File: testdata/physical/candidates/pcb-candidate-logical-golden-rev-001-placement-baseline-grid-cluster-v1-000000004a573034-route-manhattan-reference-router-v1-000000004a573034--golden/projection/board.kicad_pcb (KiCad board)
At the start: 2 copper layers, 60 x 40 mm, 6 parts

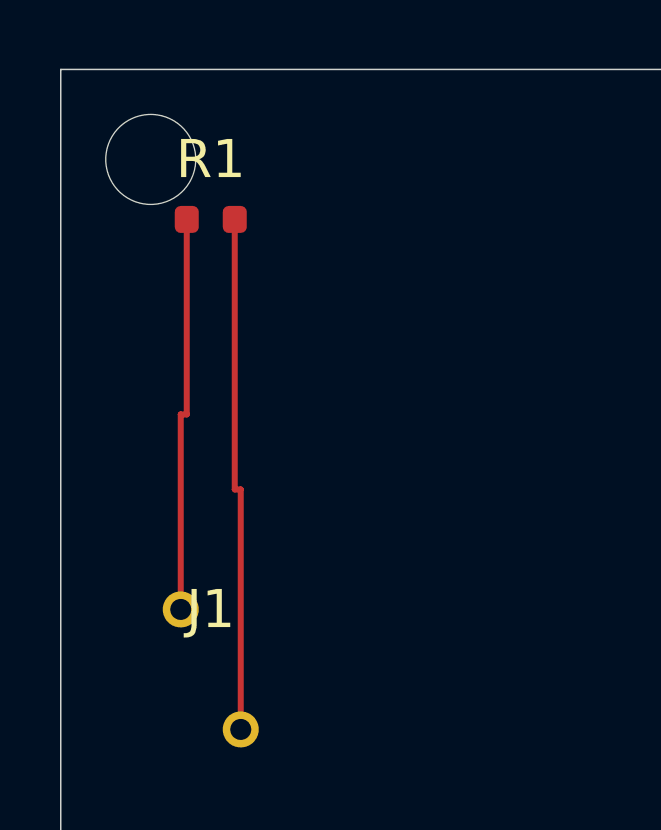
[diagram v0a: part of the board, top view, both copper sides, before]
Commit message: fix(pcb): pass pinned KiCad 10 fabrication gates
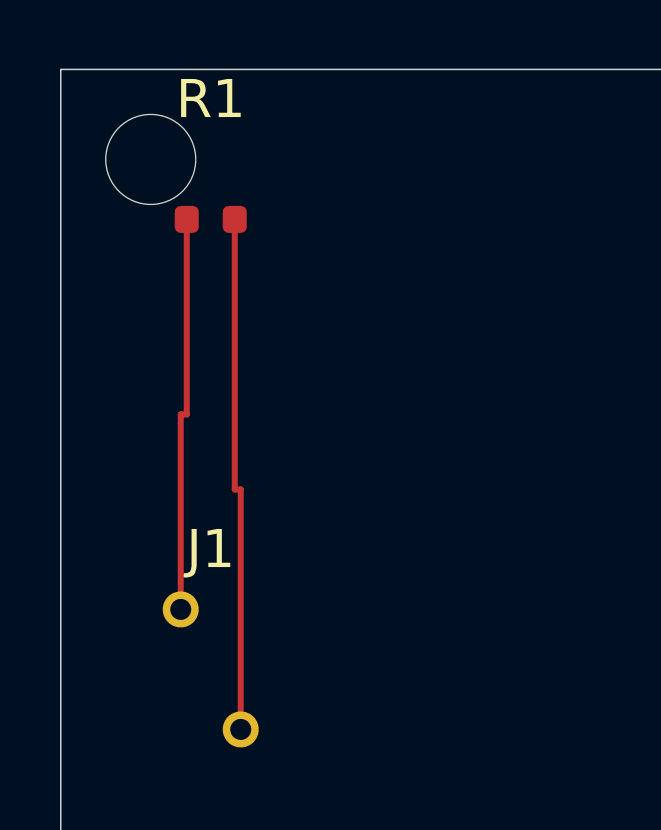
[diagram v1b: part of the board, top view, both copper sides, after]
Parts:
- ? (x4): footprint Jingwei:MechanicalHole -> (none)
- J1: footprint Jingwei:CONN_2P_2.54 -> (none)
- R1: footprint Jingwei:R_0603_1608Metric -> (none)
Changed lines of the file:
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@@
-(kicad_pcb (version 20240108) (generator jingwei-agent) (generator_version "jingwei-kicad-pcb-v1") (general (thickness 1.6)) (layers (0 "F.Cu" signal) (2 "B.Cu" signal) (36 "F.Mask" user) (37 "B.Mask" user) (37 "F.SilkS" user) (36 "B.SilkS" user) (44 "Edge.Cuts" user)) (setup) (net 1 "GND") (net 2 "+3V3") (gr_line (start 0 0) (end 60 0) (stroke (width 0.05)) (layer "Edge.Cuts")) (gr_line (start 60 0) (end 60 40) (stroke (width 0.05)) (layer "Edge.Cuts")) (gr_line (start 60 40) (end 0 40) (stroke (width 0.05)) (layer "Edge.Cuts")) (gr_line (start 0 40) (end 0 0) (stroke (width 0.05)) (layer "Edge.Cuts")) (footprint "Jingwei:MechanicalHole" (layer "F.Cu") (at 3 3) (pad "" np_thru_hole circle (at 0 0) (size 3 3) (drill 3) (layers "*.Cu" "*.Mask"))) (footprint "Jingwei:MechanicalHole" (layer "F.Cu") (at 57 3) (pad "" np_thru_hole circle (at 0 0) (size 3 3) (drill 3) (layers "*.Cu" "*.Mask"))) (footprint "Jingwei:MechanicalHole" (layer "F.Cu") (at 3 37) (pad "" np_thru_hole circle (at 0 0) (size 3 3) (drill 3) (layers "*.Cu" "*.Mask"))) (footprint "Jingwei:MechanicalHole" (layer "F.Cu") (at 57 37) (pad "" np_thru_hole circle (at 0 0) (size 3 3) (drill 3) (layers "*.Cu" "*.Mask"))) (footprint "Jingwei:CONN_2P_2.54" (layer "F.Cu") (at 5 20) (property "Reference" "J1" (at 0 -2) (layer "F.SilkS")) (property "JINGWEI_ID" "pcb-footprint:component:J1" (at 0 0) (layer "F.Fab" hide)) (pad "1" thru_hole circle (at -1 -2) (size 1.2 1.2) (drill 0.7) (layers "*.Cu" "*.Mask") (net 2 "+3V3")) (pad "2" thru_hole circle (at 1 2) (size 1.2 1.2) (drill 0.7) (layers "*.Cu" "*.Mask") (net 1 "GND"))) (footprint "Jingwei:R_0603_1608Metric" (layer "F.Cu") (at 5 5) (property "Reference" "R1" (at 0 -2) (layer "F.SilkS")) (property "JINGWEI_ID" "pcb-footprint:component:R1" (at 0 0) (layer "F.Fab" hide)) (pad "1" smd roundrect (at -0.8 0) (size 0.8 0.9) (layers "F.Cu" "F.Paste" "F.Mask") (roundrect_rratio 0.25) (net 2 "+3V3")) (pad "2" smd roundrect (at 0.8 0) (size 0.8 0.9) (layers "F.Cu" "F.Paste" "F.Mask") (roundrect_rratio 0.25) (net 1 "GND"))) (segment (start 4 18) (end 4 11.5) (width 0.2) (layer "F.Cu") (net 2)) (segment (start 4 11.5) (end 4.2 11.5) (width 0.2) (layer "F.Cu") (net 2)) (segment (start 4.2 11.5) (end 4.2 5) (width 0.2) (layer "F.Cu") (net 2)) (segment (start 6 22) (end 6 14) (width 0.2) (layer "F.Cu") (net 1)) (segment (start 6 14) (end 5.8 14) (width 0.2) (layer "F.Cu") (net 1)) (segment (start 5.8 14) (end 5.8 5) (width 0.2) (layer "F.Cu") (net 1)))
+(kicad_pcb (version 20250513) (generator jingwei-agent) (generator_version "jingwei-kicad-pcb-v1") (general (thickness 1.6)) (layers (0 "F.Cu" signal) (2 "B.Cu" signal) (9 "F.Adhes" user) (11 "B.Adhes" user) (13 "F.Paste" user) (15 "B.Paste" user) (5 "F.SilkS" user) (7 "B.SilkS" user) (1 "F.Mask" user) (3 "B.Mask" user) (17 "Dwgs.User" user) (19 "Cmts.User" user) (21 "Eco1.User" user) (23 "Eco2.User" user) (25 "Edge.Cuts" user) (27 "Margin" user) (31 "F.CrtYd" user) (29 "B.CrtYd" user) (35 "F.Fab" user) (33 "B.Fab" user)) (setup) (net 1 "GND") (net 2 "+3V3") (gr_line (start 0 0) (end 60 0) (stroke (width 0.05)) (layer "Edge.Cuts")) (gr_line (start 60 0) (end 60 40) (stroke (width 0.05)) (layer "Edge.Cuts")) (gr_line (start 60 40) (end 0 40) (stroke (width 0.05)) (layer "Edge.Cuts")) (gr_line (start 0 40) (end 0 0) (stroke (width 0.05)) (layer "Edge.Cuts")) (footprint "" (layer "F.Cu") (at 3 3) (pad "" np_thru_hole circle (at 0 0) (size 3 3) (drill 3) (layers "*.Cu" "*.Mask"))) (footprint "" (layer "F.Cu") (at 57 3) (pad "" np_thru_hole circle (at 0 0) (size 3 3) (drill 3) (layers "*.Cu" "*.Mask"))) (footprint "" (layer "F.Cu") (at 3 37) (pad "" np_thru_hole circle (at 0 0) (size 3 3) (drill 3) (layers "*.Cu" "*.Mask"))) (footprint "" (layer "F.Cu") (at 57 37) (pad "" np_thru_hole circle (at 0 0) (size 3 3) (drill 3) (layers "*.Cu" "*.Mask"))) (footprint "" (layer "F.Cu") (at 5 20) (property "Reference" "J1" (at 0 -4) (layer "F.SilkS")) (property "JINGWEI_FOOTPRINT" "CONN_2P_2.54" (at 0 0) (layer "F.Fab") (hide yes)) (property "JINGWEI_ID" "pcb-footprint:component:J1" (at 0 0) (layer "F.Fab") (hide yes)) (pad "1" thru_hole circle (at -1 -2) (size 1.2 1.2) (drill 0.7) (layers "*.Cu" "*.Mask") (net 2 "+3V3")) (pad "2" thru_hole circle (at 1 2) (size 1.2 1.2) (drill 0.7) (layers "*.Cu" "*.Mask") (net 1 "GND"))) (footprint "" (layer "F.Cu") (at 5 5) (property "Reference" "R1" (at 0 -4) (layer "F.SilkS")) (property "JINGWEI_FOOTPRINT" "R_0603_1608Metric" (at 0 0) (layer "F.Fab") (hide yes)) (property "JINGWEI_ID" "pcb-footprint:component:R1" (at 0 0) (layer "F.Fab") (hide yes)) (pad "1" smd roundrect (at -0.8 0) (size 0.8 0.9) (layers "F.Cu" "F.Paste" "F.Mask") (roundrect_rratio 0.25) (net 2 "+3V3")) (pad "2" smd roundrect (at 0.8 0) (size 0.8 0.9) (layers "F.Cu" "F.Paste" "F.Mask") (roundrect_rratio 0.25) (net 1 "GND"))) (segment (start 4 18) (end 4 11.5) (width 0.2) (layer "F.Cu") (net 2)) (segment (start 4 11.5) (end 4.2 11.5) (width 0.2) (layer "F.Cu") (net 2)) (segment (start 4.2 11.5) (end 4.2 5) (width 0.2) (layer "F.Cu") (net 2)) (segment (start 6 22) (end 6 14) (width 0.2) (layer "F.Cu") (net 1)) (segment (start 6 14) (end 5.8 14) (width 0.2) (layer "F.Cu") (net 1)) (segment (start 5.8 14) (end 5.8 5) (width 0.2) (layer "F.Cu") (net 1)))
